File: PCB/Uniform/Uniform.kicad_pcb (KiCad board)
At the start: 2 copper layers, 301.5 x 93.4 mm, 164 parts, among them CON1 826629-5, CON2 Conn_01x03, U1 STM32L072KZT6

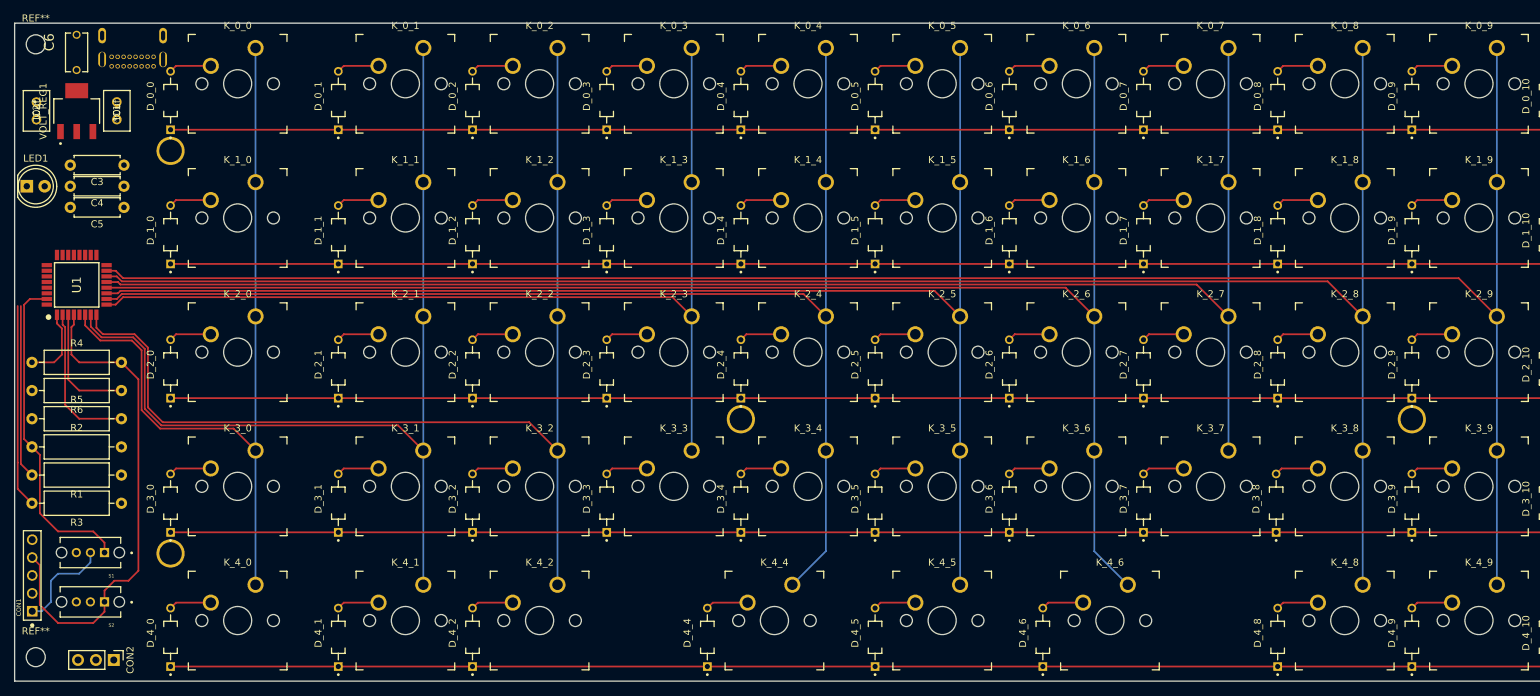
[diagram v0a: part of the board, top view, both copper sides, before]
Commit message: re-worked layout to reduce ratsnest crossover
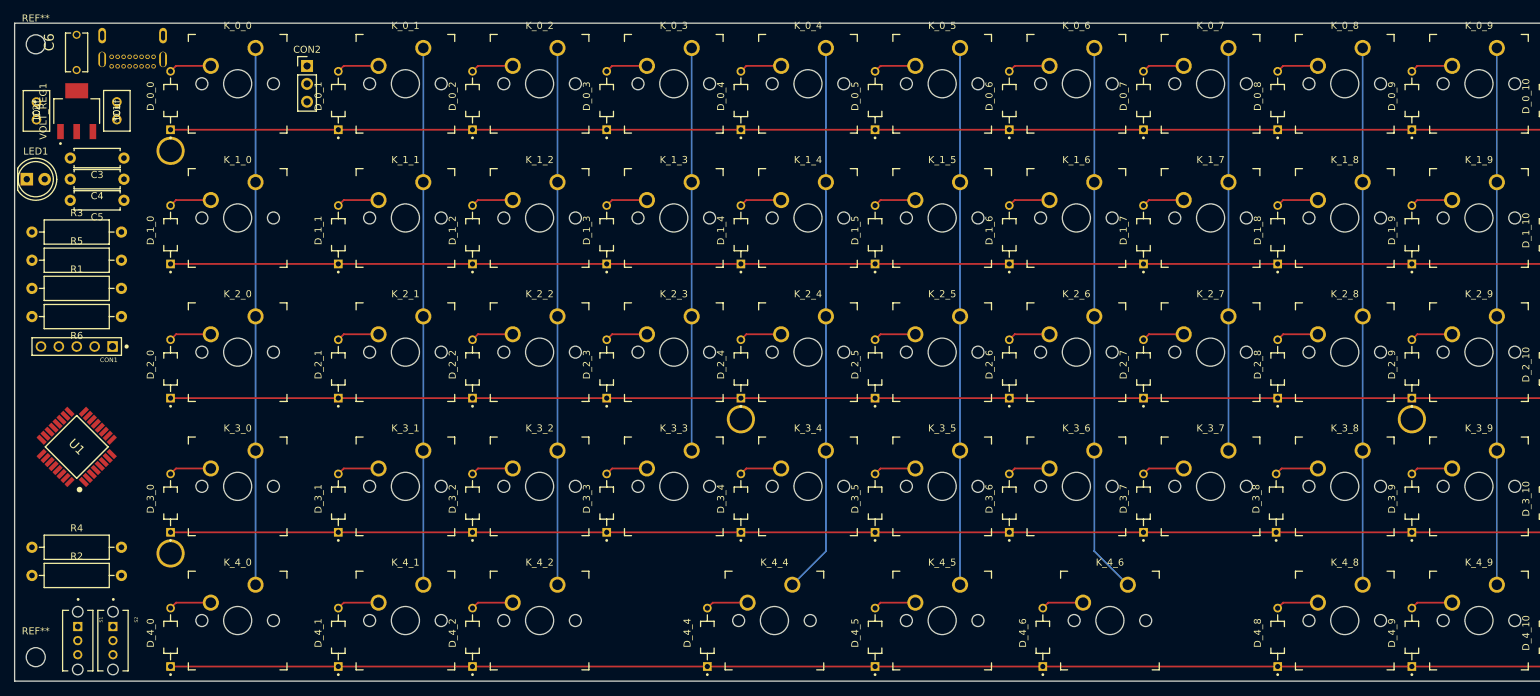
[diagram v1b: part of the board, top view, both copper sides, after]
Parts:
- moved CON2 88.7 mm to (81.3, 111.8), turned to 0 degrees
- moved R3 40.5 mm to (42.2, 135.3), turned to 0 degrees
- moved CON1 39.3 mm to (53.7, 151.6), turned to 180 degrees
- moved R1 29.4 mm to (42.2, 143.3), turned to 0 degrees
- moved R4 26.2 mm to (42.2, 180.1)
- moved U1 23.0 mm to (48.6, 165.8), turned to 135 degrees
- moved R5 22.5 mm to (42.2, 139.3)
- moved R2 18.2 mm to (42.2, 184.1)
- moved S1 12.6 mm to (48.7, 193.3), turned to -90 degrees
- moved R6 10.5 mm to (54.9, 147.3)
- moved S2 6.36 mm to (53.7, 193.3), turned to -90 degrees
- moved C3 1.00 mm to (55.3, 124.8)
- moved C4 1.00 mm to (55.3, 127.8)
- moved C5 1.00 mm to (55.3, 130.8)
- moved LED1 1.00 mm to (41.5, 127.8)
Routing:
- net C9: track 276.2 -> 76.2 mm
- net C8: track 256.9 -> 76.2 mm
- net C7: track 218.4 -> 57.2 mm
- net C6: track 220.1 -> 78.2 mm
- net C5: track 199.0 -> 76.2 mm
- net C4: track 181.9 -> 78.2 mm
- net C3: track 141.8 -> 57.2 mm
- net C2: track 155.7 -> 76.2 mm
- net RESET: track 71.0 -> 0.00 mm
- net C1: track 137.4 -> 76.2 mm
- net BOOT: track 46.4 -> 0.00 mm
- net C0: track 114.2 -> 76.2 mm
- net Net-(R3-Pad2): track 28.8 -> 0.00 mm
- net +3V3: track 24.9 -> 0.00 mm
- net Net-(R1-Pad2): track 24.7 -> 0.00 mm
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
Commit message: PCB first pass complete
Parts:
- LED1: footprint LED_THT:LED_D5.0mm_Clear -> LED_THT:LED_D3.0mm_Clear
- moved LED2 35.4 mm to (55.4, 135.9)
- moved C6 29.4 mm to (41.6, 138.4)
- moved R1 26.0 mm to (42.1, 117.4)
- moved LED1 20.8 mm to (49.7, 108.7), turned to 180 degrees
- moved C3 19.7 mm to (44.7, 141.5), turned to 0 degrees
- moved R3 14.0 mm to (42.1, 121.4)
- moved R5 13.8 mm to (54.8, 145.2), turned to 180 degrees
- moved C5 13.0 mm to (44.7, 138.4), turned to 0 degrees
- moved R2 13.0 mm to (54.8, 180.9), turned to 180 degrees
- moved C4 12.9 mm to (44.7, 135.3), turned to 0 degrees
- moved V_REG 9.71 mm to (48.4, 127.9)
- moved C1 8.59 mm to (54.1, 128.0)
- moved C2 8.59 mm to (42.7, 125.5)
- moved S1 7.70 mm to (48.5, 185.7), turned to 180 degrees
- moved S2 5.82 mm to (48.5, 190.9), turned to 180 degrees
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- renumbered REF** to EM1, REF** to EM2, CON2 to LED2, VOLT_REG1 to V_REG
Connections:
- U1 pad 2: LED_DATA -> R4
- U1 pad 25: C13 -> STATUS_LED_DATA
- U1 pad 26: R4 -> LED_DATA
- U1 pad 27: R3 -> R0
- U1 pad 28: R2 -> R1
- U1 pad 29: R1 -> C13
- U1 pad 3: STATUS_LED_DATA -> R3
- U1 pad 30: R0 -> R2
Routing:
- net C13: track 78.2 -> 397.4 mm, vias 0 -> 2
- net C12: track 81.1 -> 366.4 mm
- net C11: track 80.1 -> 340.2 mm
- net C10: track 76.2 -> 315.8 mm
- net C9: track 76.2 -> 279.3 mm
- net GND: track 0.00 -> 196.6 mm, vias 0 -> 1
- net C8: track 76.2 -> 259.5 mm
- net C7: track 57.2 -> 220.7 mm
- net C6: track 78.2 -> 222.0 mm
- net +3V3: track 0.00 -> 134.3 mm, vias 0 -> 3
- net C5: track 76.2 -> 200.3 mm
- net C4: track 78.2 -> 182.5 mm
- net C3: track 57.2 -> 141.7 mm
- net RESET: track 0.00 -> 77.0 mm, vias 0 -> 1
- net R0: track 257.2 -> 325.8 mm, vias 0 -> 1
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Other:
- outline, holes or cut-outs redrawn
- board text added: "BOOT->"
- board text added: "RESET->"

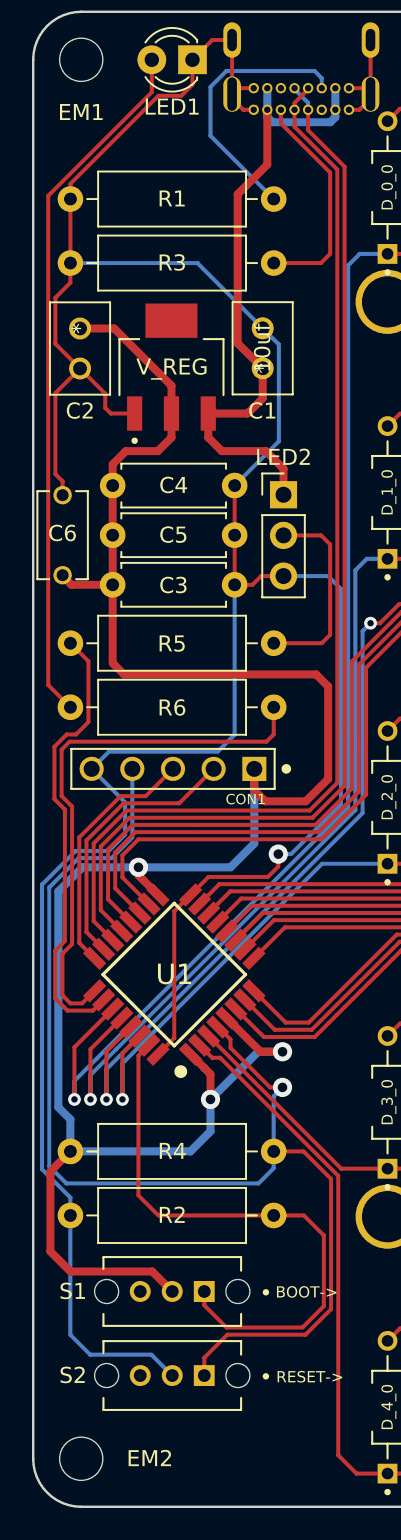
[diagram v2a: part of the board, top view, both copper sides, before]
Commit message: Added SWD silkscreen
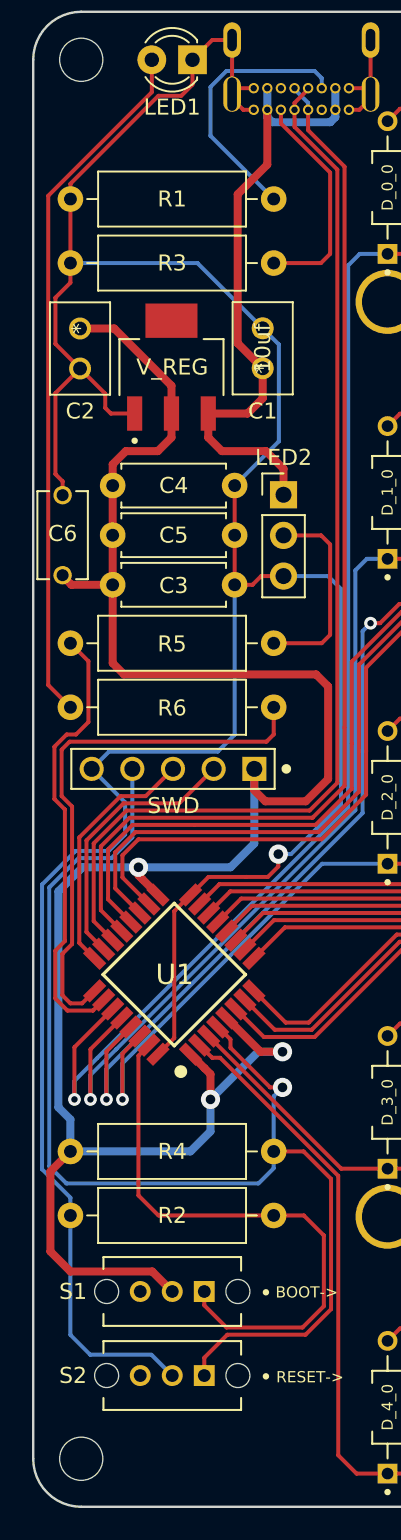
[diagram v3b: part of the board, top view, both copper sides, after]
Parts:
- renumbered CON1 to SWD
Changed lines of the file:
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@@
     (property "Sheetname" "")
     (attr through_hole)
-    (fp_text reference "CON1" (at 0.532828 -1.909362) (layer "F.SilkS")
-      (effects (font (size 0.640994 0.640994) (thickness 0.15)))
+    (fp_text reference "SWD" (at 5.05 -2.3) (layer "F.SilkS")
+      (effects (font (size 1 1) (thickness 0.15)))
     )
     (fp_text value "826629-5" (at 3.019904 9.995016) (layer "F.Fab")
@@
     (tags "mounting hole 2.7mm no annular m2.5")
     (attr exclude_from_pos_files exclude_from_bom)
-    (fp_text reference "EM1" (at 0 3.3) (layer "F.SilkS")
+    (fp_text reference "EM1" (at 0 -5.3) (layer "Dwgs.User") hide
       (effects (font (size 1 1) (thickness 0.15)))
     )
@@
     (tags "mounting hole 2.7mm no annular m2.5")
     (attr exclude_from_pos_files exclude_from_bom)
-    (fp_text reference "EM2" (at 4.2875 0) (layer "F.SilkS")
+    (fp_text reference "EM2" (at 0.0625 4.9) (layer "Dwgs.User") hide
       (effects (font (size 1 1) (thickness 0.15)))
     )

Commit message: silkscreen artwork added
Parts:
- added G***: LOGO, Graphics:graphic_logo, F.Cu at (48.6, 156.7)
- added G***: LOGO, Graphics:graphic_designed-by, B.Cu at (55.7, 194.1)
- moved LED1 3.30 mm to (49.7, 112.0)
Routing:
- net GND: track 196.6 -> 197.8 mm
- net Net-(LED1-Pad2): track 43.7 -> 43.0 mm
